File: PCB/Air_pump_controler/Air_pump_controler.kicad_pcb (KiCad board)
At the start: 2 copper layers, 24 x 24 mm, 27 parts, among them J1 Conn_01x03_Pin, J2 USB IN, J4 Motor_conn, Q1 AP30N03DF, U1 CH32V003F4U6

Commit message: Readme
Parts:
- added REF**: OSHW-Logo2_7.3x6mm_SilkScreen, Symbol:OSHW-Logo2_7.3x6mm_SilkScreen, B.Cu at (157.4, 88.2)

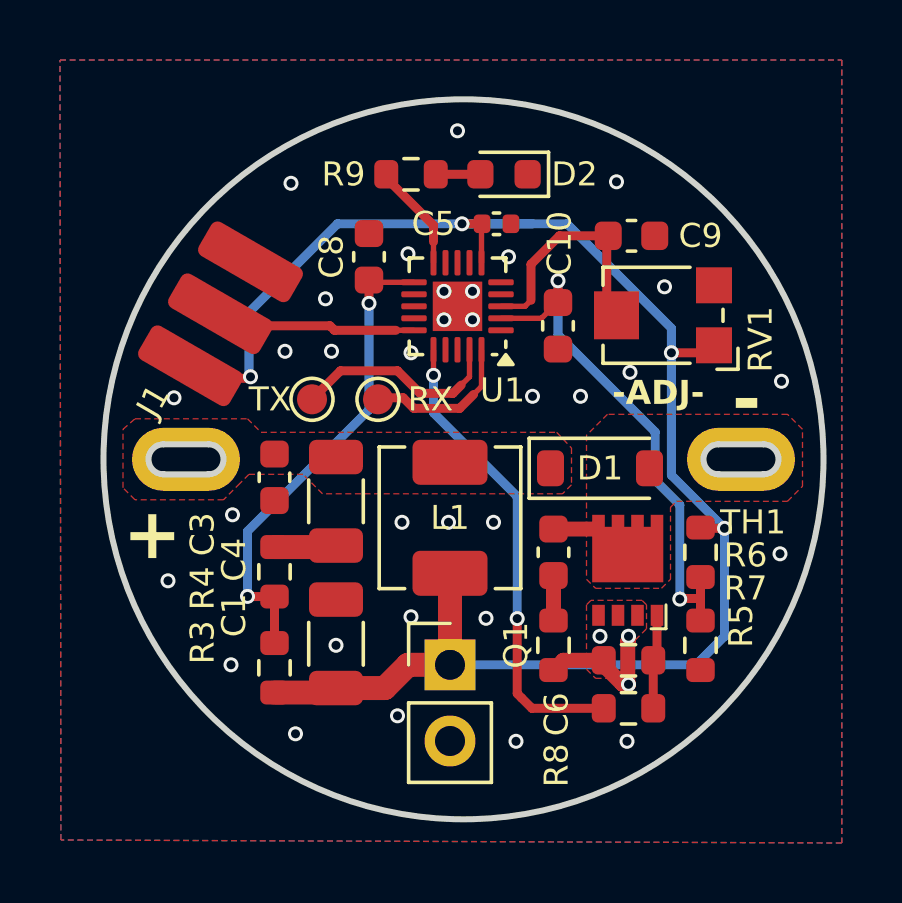
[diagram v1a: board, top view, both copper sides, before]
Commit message: Update
modified potenciometer to voltage divider
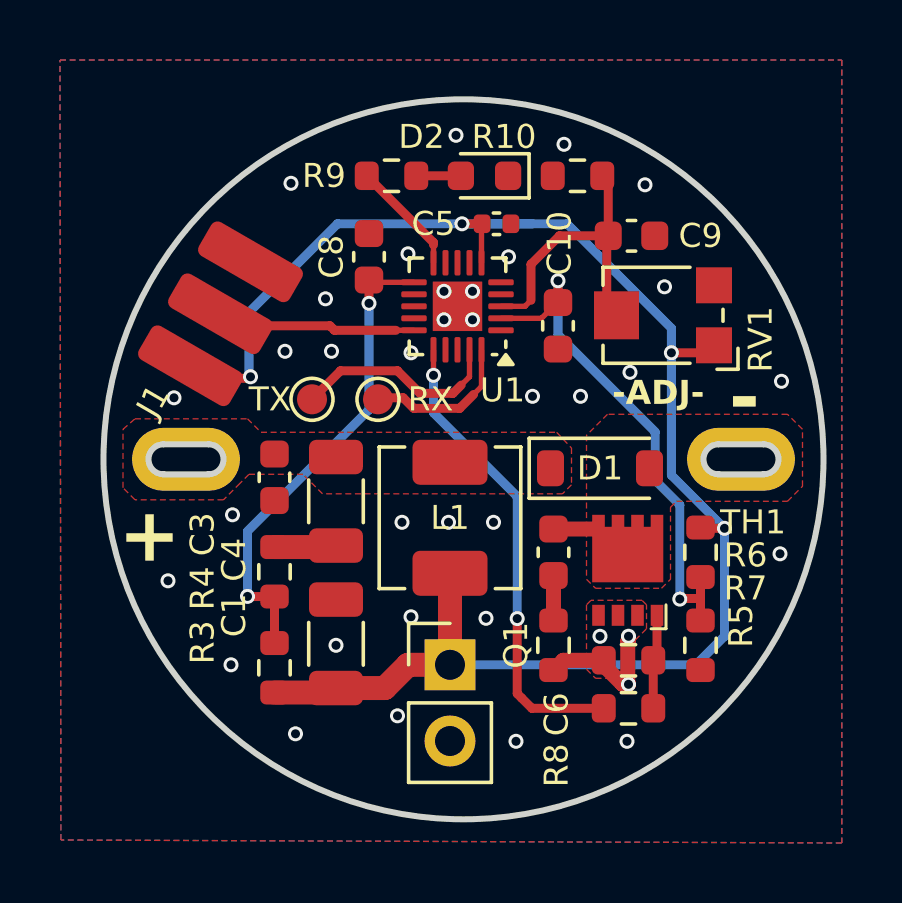
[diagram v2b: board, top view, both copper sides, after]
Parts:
- added R10: 2k, Resistor_SMD:R_0603_1608Metric, F.Cu at (161.2, 79.8)
- R4: value 10k -> 100k
- RV1: value 20k -> 50k
- moved D2 0.65 mm to (158.1, 79.8)
- moved R9 0.65 mm to (155.0, 79.8)
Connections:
- RV1 pad 3: GND -> unconnected-(RV1-Pad3)
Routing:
- net /AN_POT: track 7.99 -> 10.1 mm
- net GND: vias 36 -> 37
